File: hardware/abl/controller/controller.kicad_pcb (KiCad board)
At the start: 4 copper layers, 56.2 x 74 mm, 29 parts, among them IC1 LSF0204PWJ, IC2 FXL6408UMX, IC3 VEML6040A3OG, IC4 FXL6408UMX, J1 SFW20S-2STE1LF, J2 Conn_02x03_Odd_Even, J3 Conn_02x03_Odd_Even, J4 PRT-14417, J5 Conn_02x04_Odd_Even, Q2 AO3401A, Q4 AO3401A, U1 INA219AxD

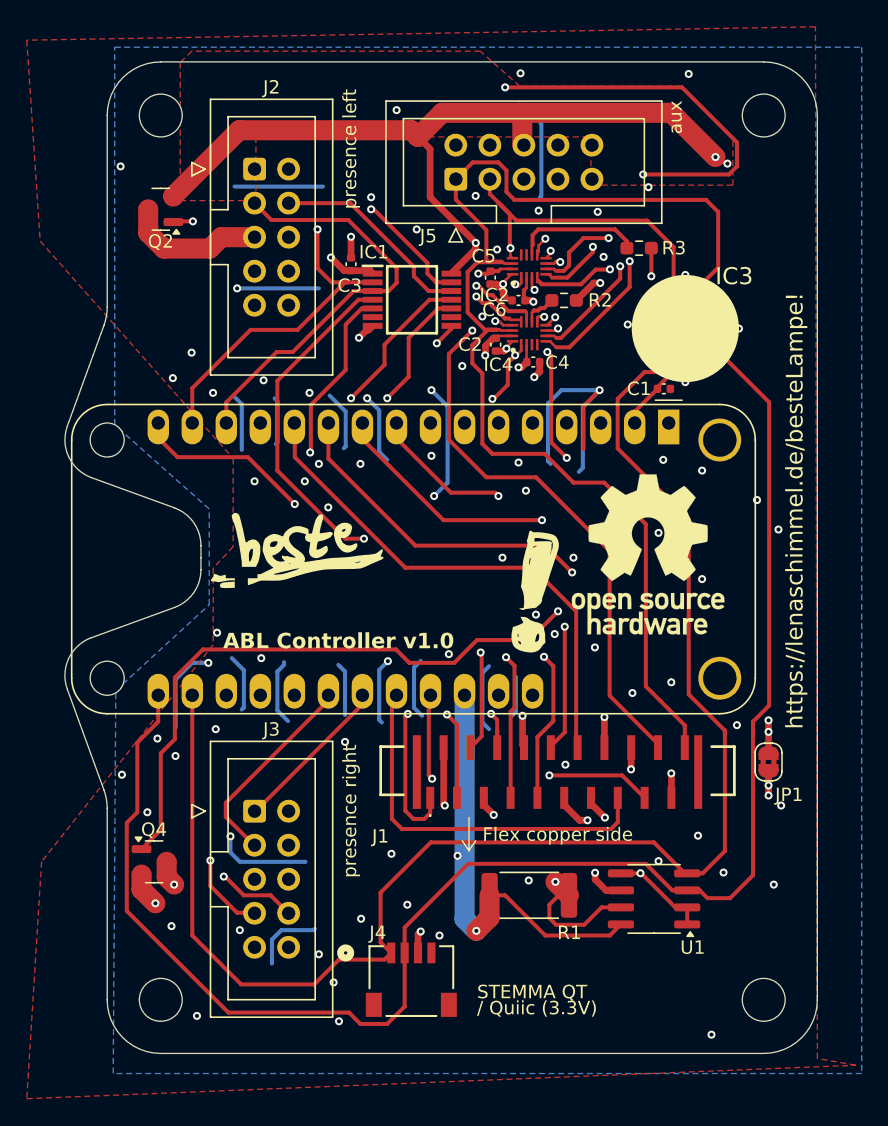
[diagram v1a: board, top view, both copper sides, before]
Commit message: Adjusted pin assignment of i1 to i4, rotated the flex connector, and rerouted most of the long traces.
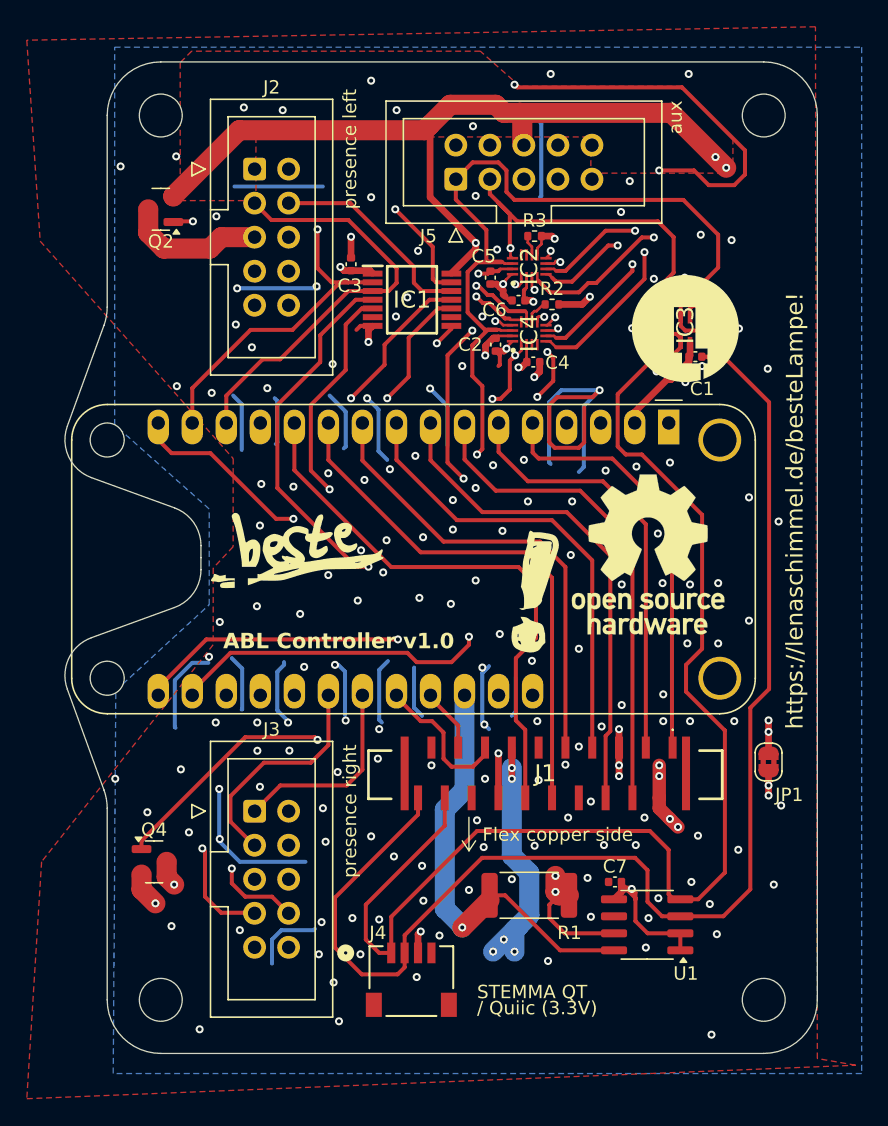
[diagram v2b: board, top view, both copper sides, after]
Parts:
- added C7: 100nF, Capacitor_SMD:C_0402_1005Metric, F.Cu at (100.9, 112.2)
- R2, R3: footprint Resistor_SMD:R_0603_1608Metric_Pad0.98x0.95mm_HandSolder -> Resistor_SMD:R_0402_1005Metric
- moved R3 7.85 mm to (94.9, 64.0)
- moved C1 3.36 mm to (106.9, 73.0)
- moved U1 2.00 mm to (103.3, 115.4)
- moved R2 0.95 mm to (96.2, 69.1)
- moved J1 0.92 mm to (95.7, 104.1), turned to 180 degrees
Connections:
- J1 pad 1: /i4 -> /i1
- J1 pad 3: /i3 -> /i2
- J1 pad 4: /i2 -> /i3
- J1 pad 6: /i1 -> /i4
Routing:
- net GND: track 240.7 -> 336.2 mm, vias 92 -> 165
- net +3.3V: track 114.1 -> 82.2 mm
- net /ALERT: track 23.7 -> 4.76 mm, vias 2 -> 0
- net /EN_LED: track 28.7 -> 10.9 mm
- net /SDA: track 215.8 -> 199.1 mm, vias 0 -> 2
- net +4V: track 116.9 -> 101.8 mm, vias 5 -> 11
- net +5V: track 168.7 -> 180.3 mm, vias 8 -> 12
- net Net-(IC2-/RST): track 9.71 -> 1.53 mm
- net /i3: track 28.8 -> 36.9 mm, vias 1 -> 0
- net (no net): track 3.96 -> 11.0 mm
- net /i2: track 25.3 -> 32.1 mm, vias 1 -> 0
- net /SCL: track 191.4 -> 185.2 mm, vias 3 -> 5
- net /FX_5_7: track 72.2 -> 66.2 mm
- net /i6: track 39.8 -> 34.7 mm, vias 2 -> 0
- net /i1: track 26.8 -> 31.8 mm, vias 1 -> 0
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
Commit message: Finally added the missing schottky diode and re-layoutet the power area.
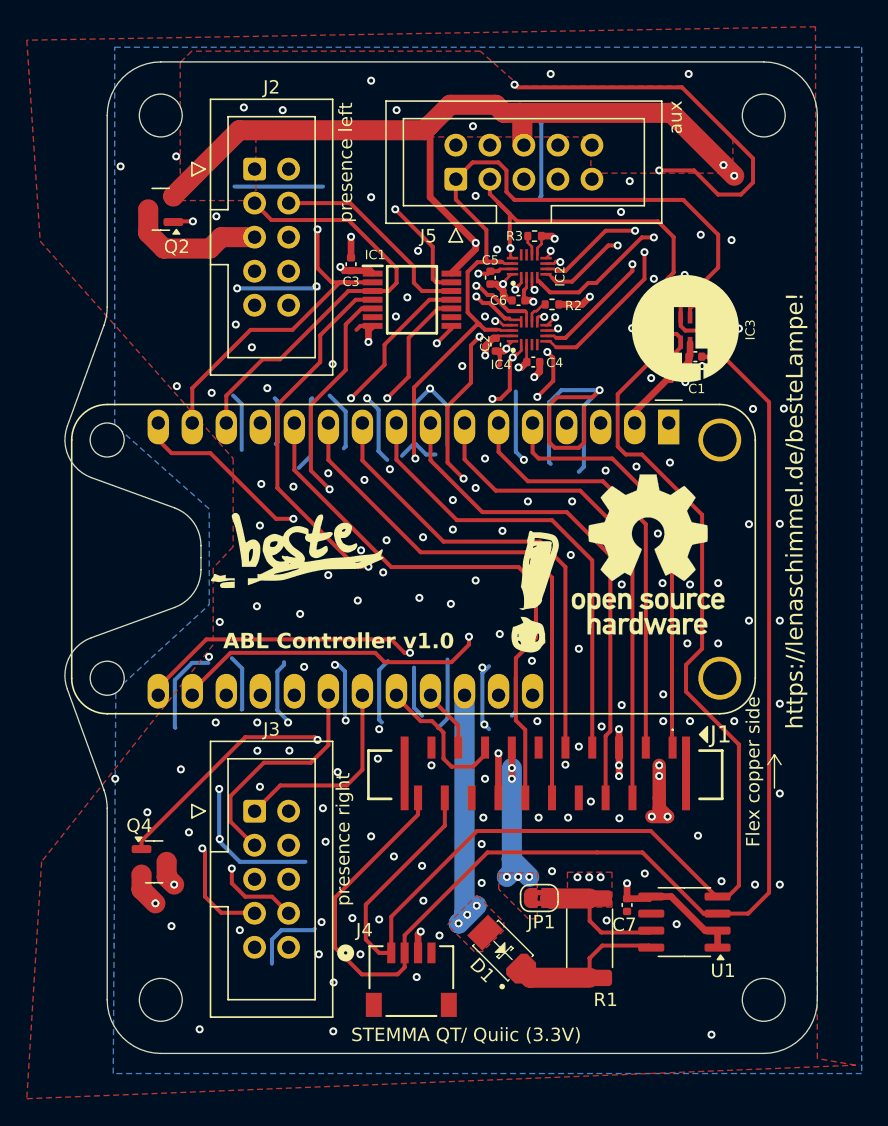
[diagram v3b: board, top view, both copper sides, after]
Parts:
- added D1: D_Schottky, Own footprints:YFW SSL34F Schottky Diode, F.Cu at (92.5, 117.3)
- moved JP1 19.9 mm to (95.2, 113.4), turned to 180 degrees
- moved R1 5.53 mm to (99.0, 116.4), turned to 90 degrees
- moved U1 2.79 mm to (106.1, 115.2)
- moved C7 1.95 mm to (101.8, 113.9), turned to 90 degrees
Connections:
- R1 pad 1: VBUS -> Net-(D1-K)
- U1 pad 8: VBUS -> Net-(D1-K)
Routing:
- net +5V: track 180.3 -> 91.5 mm, vias 12 -> 10
- net +4V: track 101.8 -> 18.4 mm, vias 11 -> 10
- net GND: track 336.2 -> 356.0 mm, vias 165 -> 159
- net VBUS: track 32.3 -> 18.4 mm, vias 1 -> 3
- net +3.3V: track 82.2 -> 68.6 mm
- net Net-(D1-K): track 0.00 -> 11.9 mm
- net (no net): track 11.0 -> 18.6 mm
- net /FX_5_6: track 76.0 -> 77.8 mm
- net /SDA: track 199.1 -> 199.9 mm
- net /SCL: track 185.2 -> 184.5 mm
- added copper zone on F.Cu, net +4V
- added copper zone on F.Cu, net VBUS

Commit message: Added pull ups for I2C.
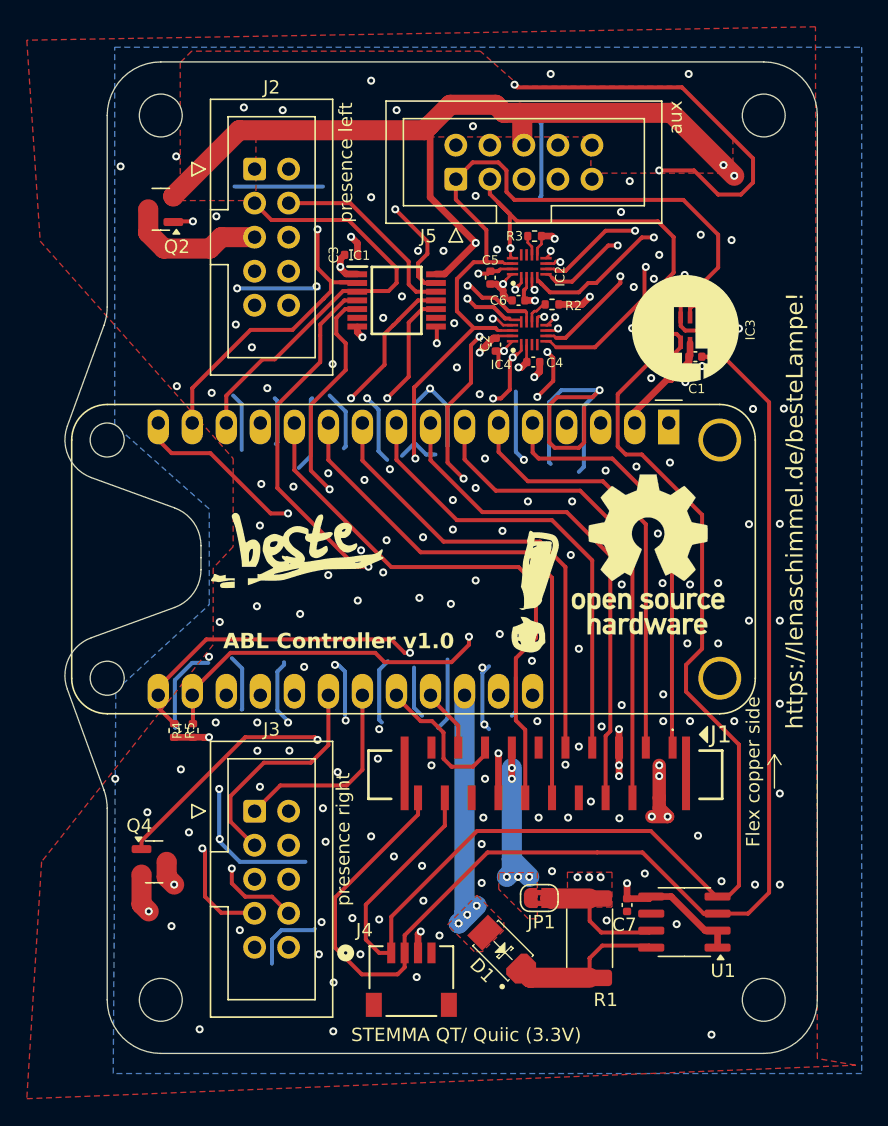
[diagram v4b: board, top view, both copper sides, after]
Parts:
- added R4: 4700R, Resistor_SMD:R_0402_1005Metric, F.Cu at (69.4, 100.9)
- added R5: 4700R, Resistor_SMD:R_0402_1005Metric, F.Cu at (68.0, 100.9)
- moved IC1 1.15 mm to (84.6, 68.8)
- moved C3 0.70 mm to (81.2, 65.4), turned to 180 degrees
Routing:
- net +3.3V: track 68.6 -> 106.2 mm, vias 10 -> 11
- net /SCL: track 184.5 -> 186.9 mm
- net /SDA: track 199.9 -> 202.1 mm
- net /TX_L: track 32.8 -> 31.4 mm
- net +5V: track 91.5 -> 92.8 mm
- net /FX_3_5: track 31.6 -> 32.5 mm
- net /RX_L_5: track 15.6 -> 14.7 mm
- net /TX_R: track 51.8 -> 51.1 mm
- net /TX_R_5: track 55.2 -> 54.5 mm
- net GND: track 356.0 -> 355.5 mm, vias 159 -> 164

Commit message: Make controller PCB ready for prototype prodution: change level shifter, re-route many traces, etc.
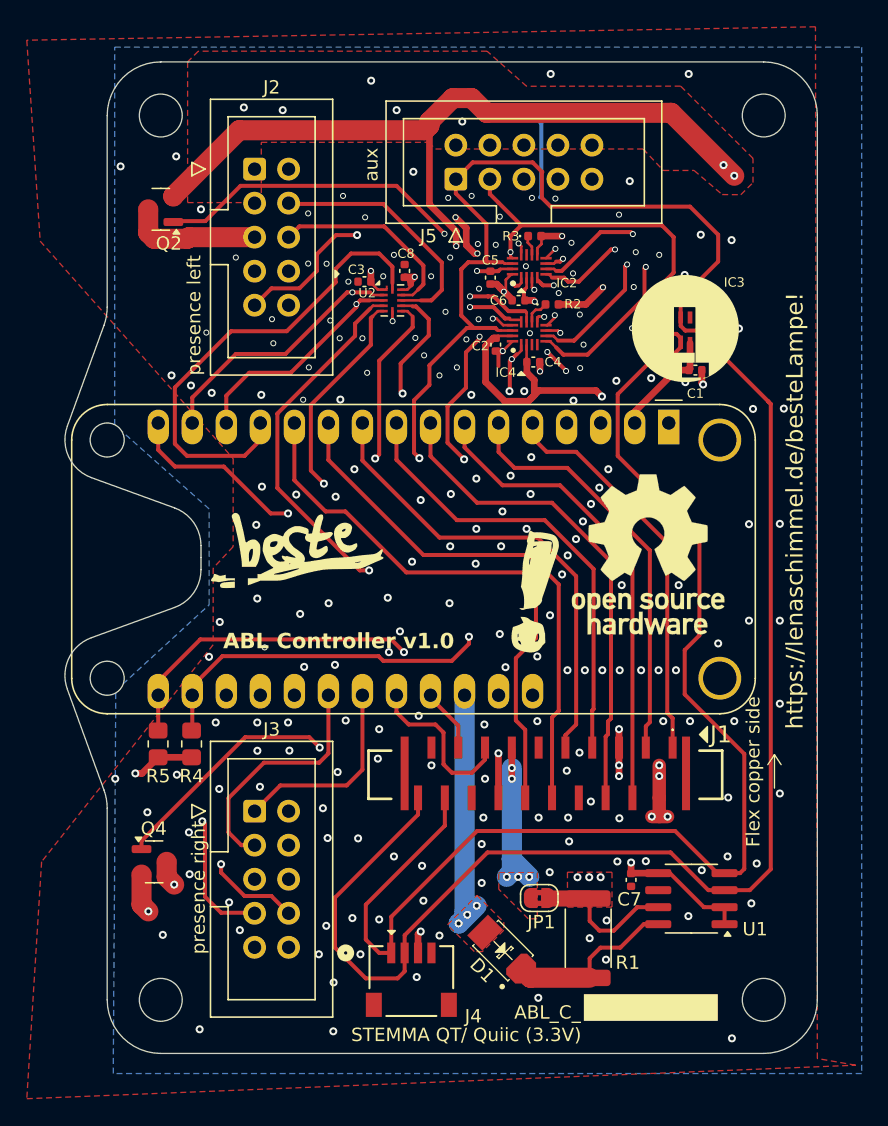
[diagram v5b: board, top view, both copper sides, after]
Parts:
- removed IC1: LSF0204PWJ, LSF0204PWJ:SOP65P640X110-14N
- added C8: 100nF, Capacitor_SMD:C_0402_1005Metric, F.Cu at (85.2, 66.6)
- added U2: TXB0104RUT, Package_DFN_QFN:Texas_R-PUQFN-N12, F.Cu at (84.3, 68.8)
- J2, J3: value Conn_02x03_Odd_Even -> Conn_02x05_Odd_Even
- J5: value Conn_02x04_Odd_Even -> Conn_02x05_Odd_Even
- R2, R3: footprint Resistor_SMD:R_0402_1005Metric -> LED_SMD:LED_0402_1005Metric
- R4, R5: footprint Resistor_SMD:R_0402_1005Metric -> Resistor_SMD:R_0805_2012Metric_Pad1.20x1.40mm_HandSolder
- moved C3 2.24 mm to (82.2, 67.4), turned to 0 degrees
- moved C7 1.90 mm to (102.1, 112.0)
- moved U1 1.82 mm to (106.6, 113.5)
- moved R5 1.56 mm to (66.8, 101.9)
- moved R4 1.00 mm to (69.3, 101.9)
- moved C1 1.00 mm to (106.9, 74.0)
- moved R1 0.11 mm to (98.9, 116.4)
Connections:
- J2 pad 9: unconnected-(J2-Pin_9-Pad9) -> /FX_5_0
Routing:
- net GND: track 355.5 -> 22.9 mm, vias 164 -> 207
- net /FX_5_6: track 77.8 -> 36.4 mm, vias 4 -> 2
- net /FX_5_0: track 0.00 -> 28.1 mm, vias 0 -> 2
- net /EN_UART: track 17.3 -> 36.3 mm, vias 1 -> 0
- net (no net): track 18.6 -> 0.00 mm
- net /FX_3_0: track 21.7 -> 28.6 mm
- net /RX_L_5: track 14.7 -> 19.0 mm
- net /SCL: track 186.9 -> 182.7 mm
- net /TX_R_5: track 54.5 -> 56.9 mm
- net +3.3V: track 106.2 -> 108.5 mm
- net /FX_5_3: track 65.1 -> 67.4 mm
- net +5V: track 92.8 -> 95.1 mm, vias 10 -> 11
- net /FX_3_3: track 78.0 -> 75.7 mm
- net /RX_L: track 31.9 -> 29.8 mm, vias 0 -> 1
- net /TX_L: track 31.4 -> 33.4 mm
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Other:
- board text added: "ABL_C_"

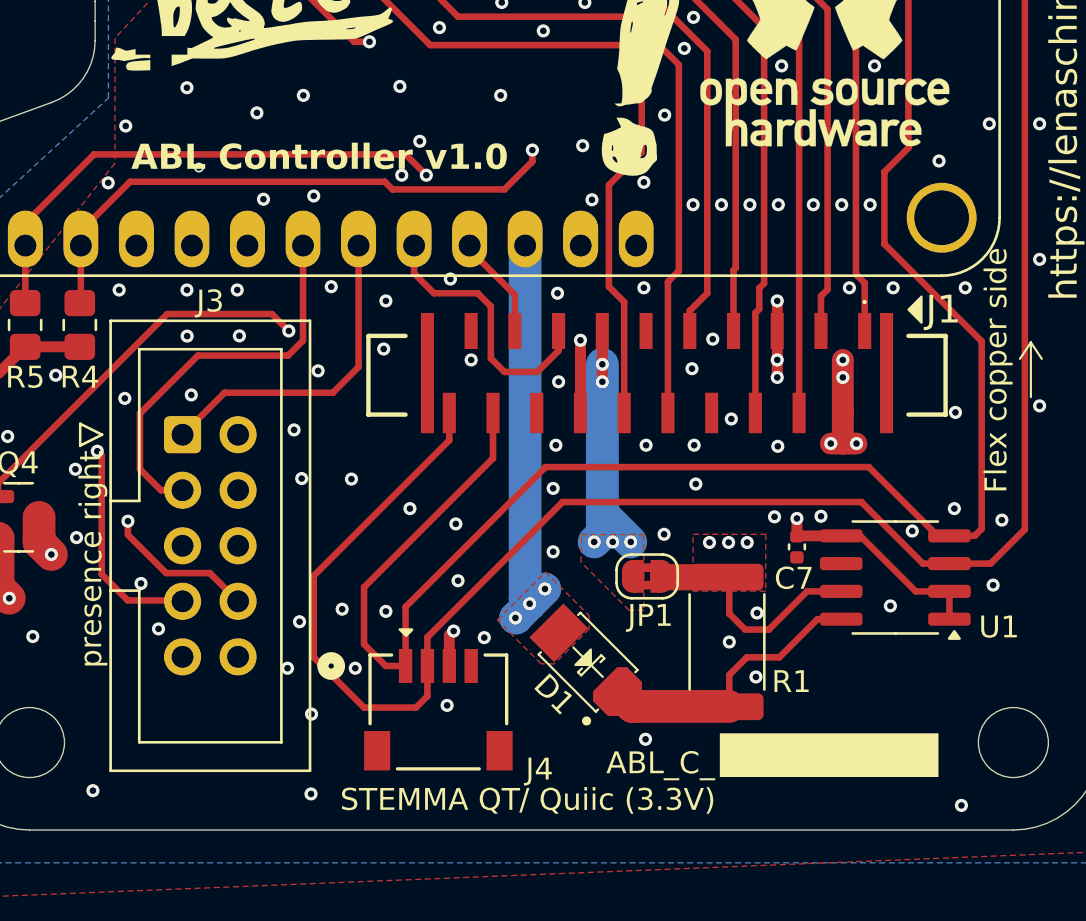
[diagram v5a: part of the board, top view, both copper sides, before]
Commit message: Fix orientation of Stemma QT / Quiic socket, add test points for voltages.
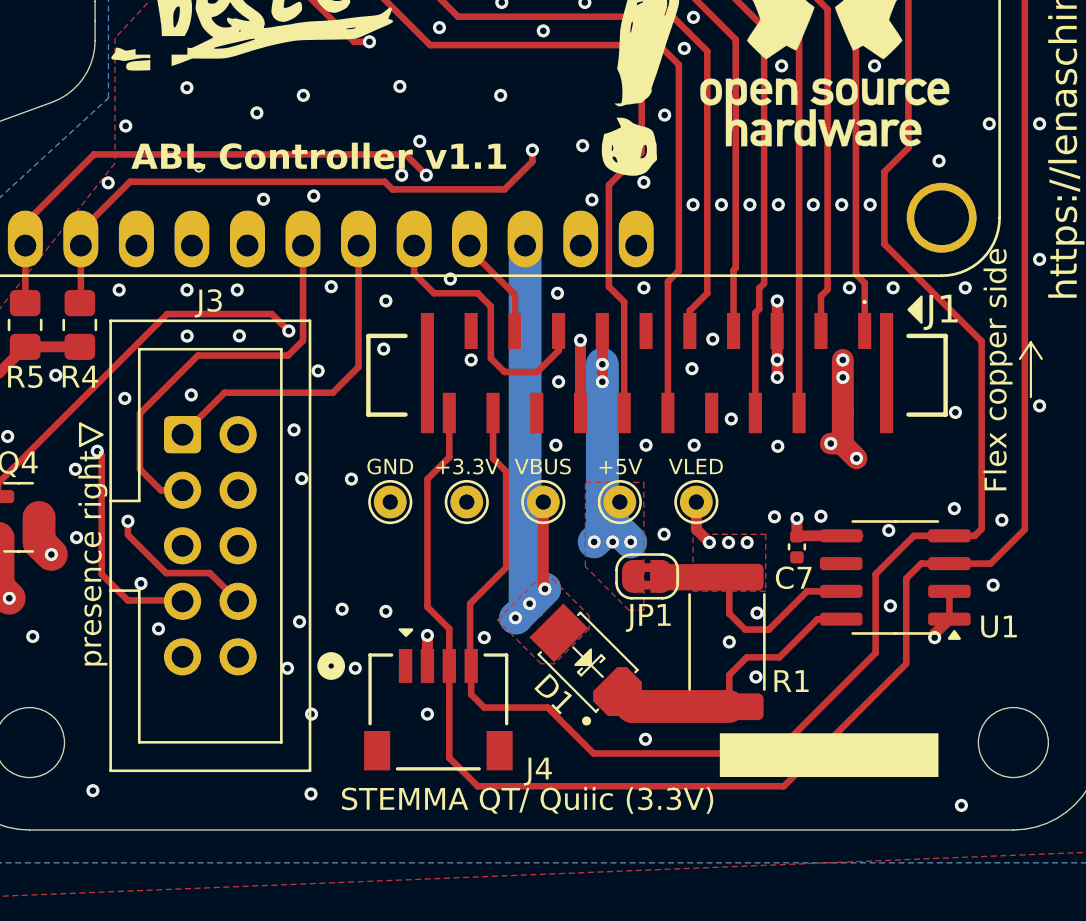
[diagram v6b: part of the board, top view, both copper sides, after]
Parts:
- added TP1: TestPoint, TestPoint:TestPoint_THTPad_D1.5mm_Drill0.7mm, F.Cu at (83.5, 110.0)
- added TP2: TestPoint, TestPoint:TestPoint_THTPad_D1.5mm_Drill0.7mm, F.Cu at (87.0, 110.0)
- added TP3: TestPoint, TestPoint:TestPoint_THTPad_D1.5mm_Drill0.7mm, F.Cu at (94.0, 110.0)
- added TP4: TestPoint, TestPoint:TestPoint_THTPad_D1.5mm_Drill0.7mm, F.Cu at (90.5, 110.0)
- added TP5: TestPoint, TestPoint:TestPoint_THTPad_D1.5mm_Drill0.7mm, F.Cu at (97.5, 110.0)
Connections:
- J4 pad 1: /SCL -> GND
- J4 pad 2: /SDA -> +3.3V
- J4 pad 3: +3.3V -> /SDA
- J4 pad 4: GND -> /SCL
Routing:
- net +3.3V: track 108.5 -> 112.8 mm, vias 11 -> 12
- net VBUS: track 18.4 -> 22.4 mm
- net /SDA: track 200.9 -> 197.0 mm
- net /SCL: track 182.7 -> 178.9 mm
- net +4V: track 19.2 -> 21.6 mm
- net GND: vias 207 -> 201
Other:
- board text added: "+3.3V"
- board text added: "+5V"
- board text added: "ABL Controller v1.1"
- board text added: "GND"
- board text added: "VBUS"
- board text added: "VLED"
- board text removed: "ABL Controller v1.0"
- board text removed: "ABL_C_"
